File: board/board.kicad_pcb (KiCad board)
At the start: 2 copper layers, 21 x 13 mm, 1 part

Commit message: initial
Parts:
- added J1: 019_100BASE-T_2x5, on_edge:on_edge_2x05_device, F.Cu at (140.0, 96.5)
- added J2: 011_GPIO, on_edge:on_edge_2x05_device, F.Cu at (140.0, 112.5)
- added J3: PoE, on_edge:on_edge_2x05_host, F.Cu at (161.0, 112.5)
- added R1: 330R, Resistor_SMD:R_0603_1608Metric, F.Cu at (146.9, 116.4)
- added R2: 330R, Resistor_SMD:R_0603_1608Metric, F.Cu at (146.8, 112.6)
- added U1: 7499211121A, b004:7499211121A, F.Cu at (147.0, 94.4)
- moved LOGO1 13.1 mm to (151.9, 112.0)
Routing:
- net GND: track 0.00 -> 39.1 mm, vias 0 -> 2
- net /PoE_GND: track 0.00 -> 36.5 mm, vias 0 -> 2
- net /eth_conn/VC1+: track 0.00 -> 33.6 mm
- net /eth_conn/LED2+: track 0.00 -> 31.1 mm, vias 0 -> 1
- net Net-(R1-Pad1): track 0.00 -> 29.7 mm, vias 0 -> 1
- net /eth_conn/LED1+: track 0.00 -> 21.2 mm, vias 0 -> 1
- net Net-(R2-Pad1): track 0.00 -> 16.8 mm, vias 0 -> 1
- net /eth_conn/RD-: track 0.00 -> 11.6 mm
- net /eth_conn/TD-: track 0.00 -> 11.4 mm
- net /eth_conn/TCT: track 0.00 -> 11.2 mm
- net /eth_conn/RD+: track 0.00 -> 8.80 mm
- net /eth_conn/RCT: track 0.00 -> 8.60 mm
- net /eth_conn/TD+: track 0.00 -> 7.84 mm
- net /eth_conn/LED2-: track 0.00 -> 3.77 mm
- net /eth_conn/LED1-: track 0.00 -> 3.64 mm
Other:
- board size 21 x 13 mm -> 21 x 29 mm
- board text added: "osf.011"
- board text added: "osf.013"
- board text added: "osf.019"
- board text added: "osf.b004.v1.0"

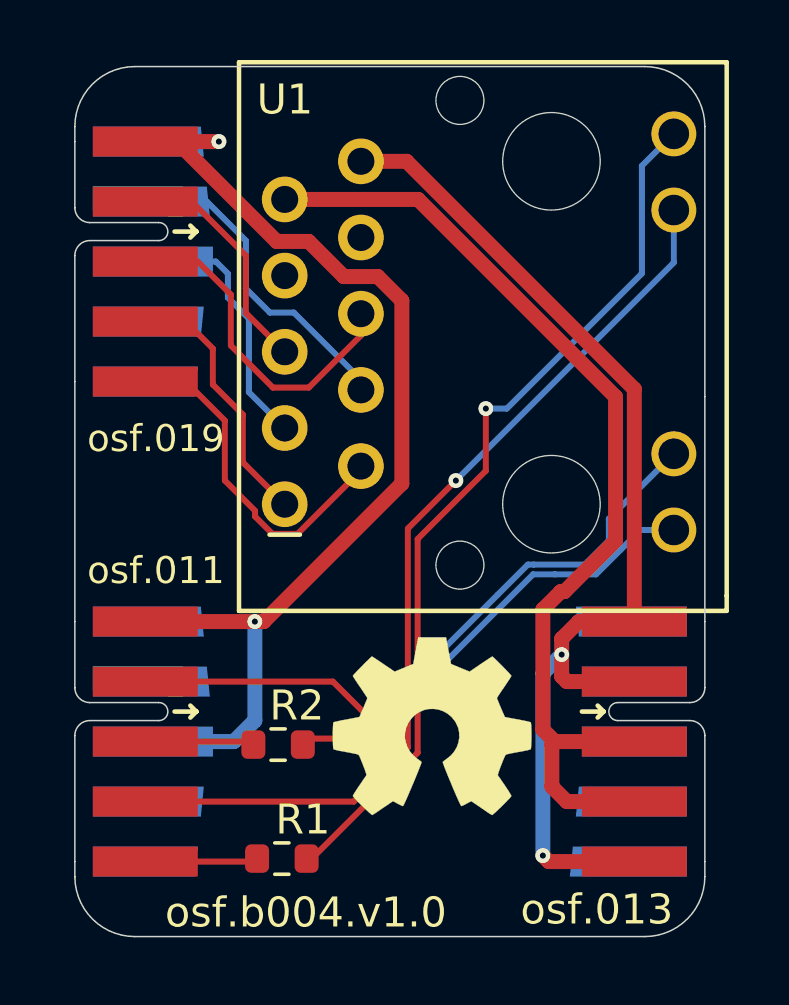
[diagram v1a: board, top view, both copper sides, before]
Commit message: modernized to new put_on_edge connectors with 3.3 and 5v
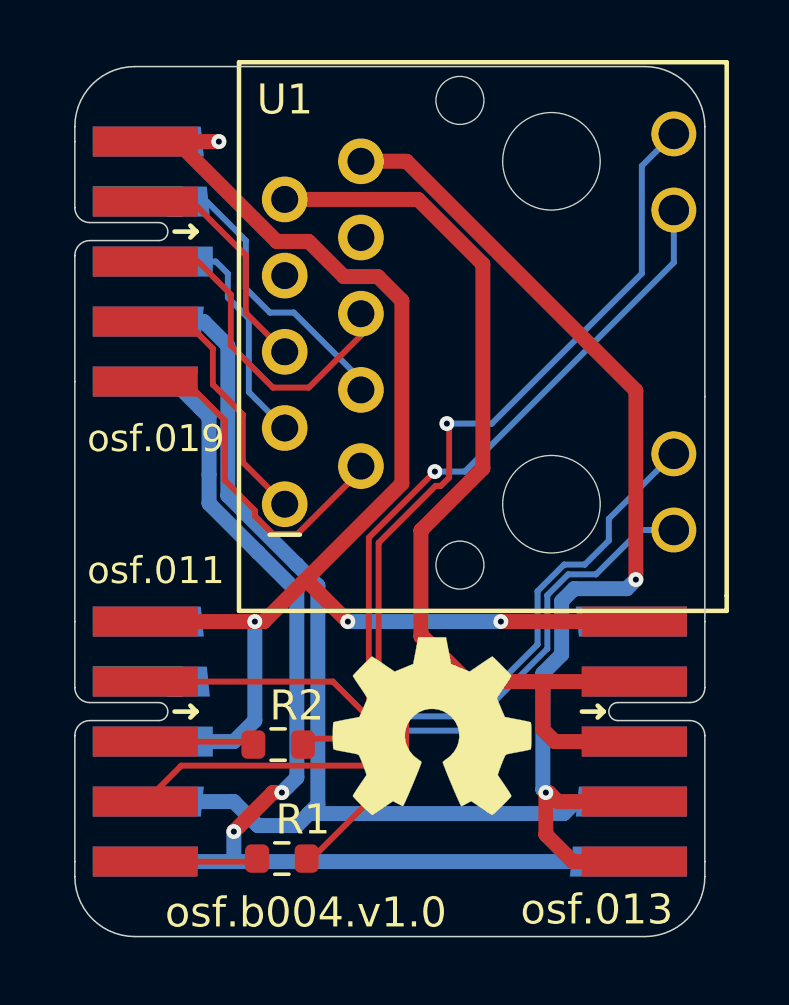
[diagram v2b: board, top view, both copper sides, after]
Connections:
- J1 pad 10: (no net) -> Net-(J2-Pad10)
- J1 pad 9: (no net) -> Net-(J2-Pad9)
- J2 pad 10: unconnected-(J2-Pad10) -> Net-(J2-Pad10)
- J2 pad 9: unconnected-(J2-Pad9) -> Net-(J2-Pad9)
- J3 pad 1: /PoE_GND -> GND
- J3 pad 10: (no net) -> Net-(J2-Pad10)
- J3 pad 2: /PoE_GND -> /eth_conn/VC1+
- J3 pad 4: /eth_conn/VC1+ -> /PoE_GND
- J3 pad 9: (no net) -> Net-(J2-Pad9)
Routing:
- net Net-(J2-Pad9): track 0.00 -> 36.9 mm
- net Net-(J2-Pad10): track 0.00 -> 35.9 mm, vias 0 -> 2
- net GND: track 39.1 -> 50.7 mm, vias 2 -> 4
- net Net-(R1-Pad1): track 29.7 -> 31.1 mm
- net /eth_conn/LED2+: track 31.1 -> 32.4 mm
- net Net-(R2-Pad1): track 16.8 -> 17.8 mm
- net /eth_conn/LED1+: track 21.2 -> 22.1 mm
- net /PoE_GND: track 36.5 -> 35.9 mm
